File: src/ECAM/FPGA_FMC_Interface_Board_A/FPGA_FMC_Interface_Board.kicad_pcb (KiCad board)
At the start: 4 copper layers, 78.7 x 63.5 mm, 78 parts, among them IC1 ATMEGA32U4TQFP, IC2 SST25VF040B-80-4I-S2AE, IC3 NCP1117ST33T3G, IC4 LD1117S12CTR, J1 5.5x2.1mm Barrel, Q1 MOSFET-NCHANNELSMD, Q2 8MHz, U1 6SLX9TQG144, U2 ASFLMB-50.000MHZ-LC-T, X1 USB-MICROB

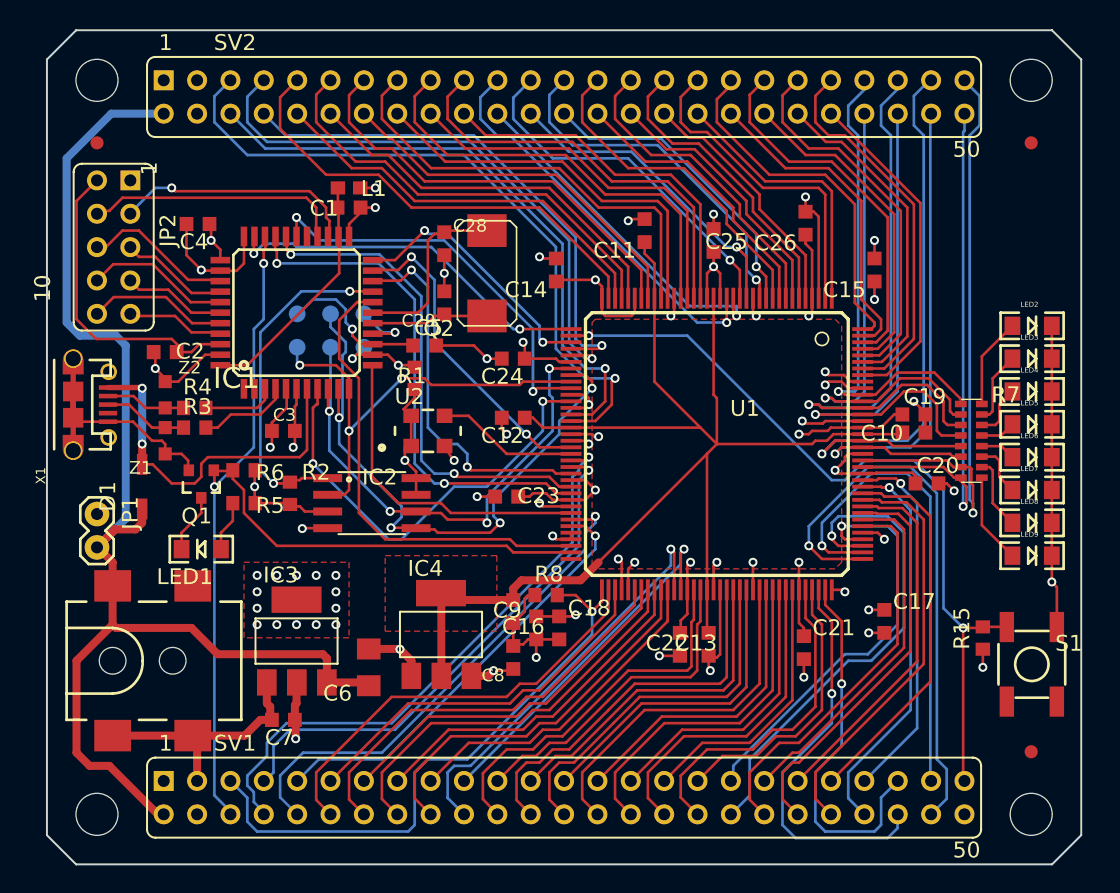
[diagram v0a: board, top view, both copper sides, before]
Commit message: added FMC connector footprint, cleaned out PCB layout
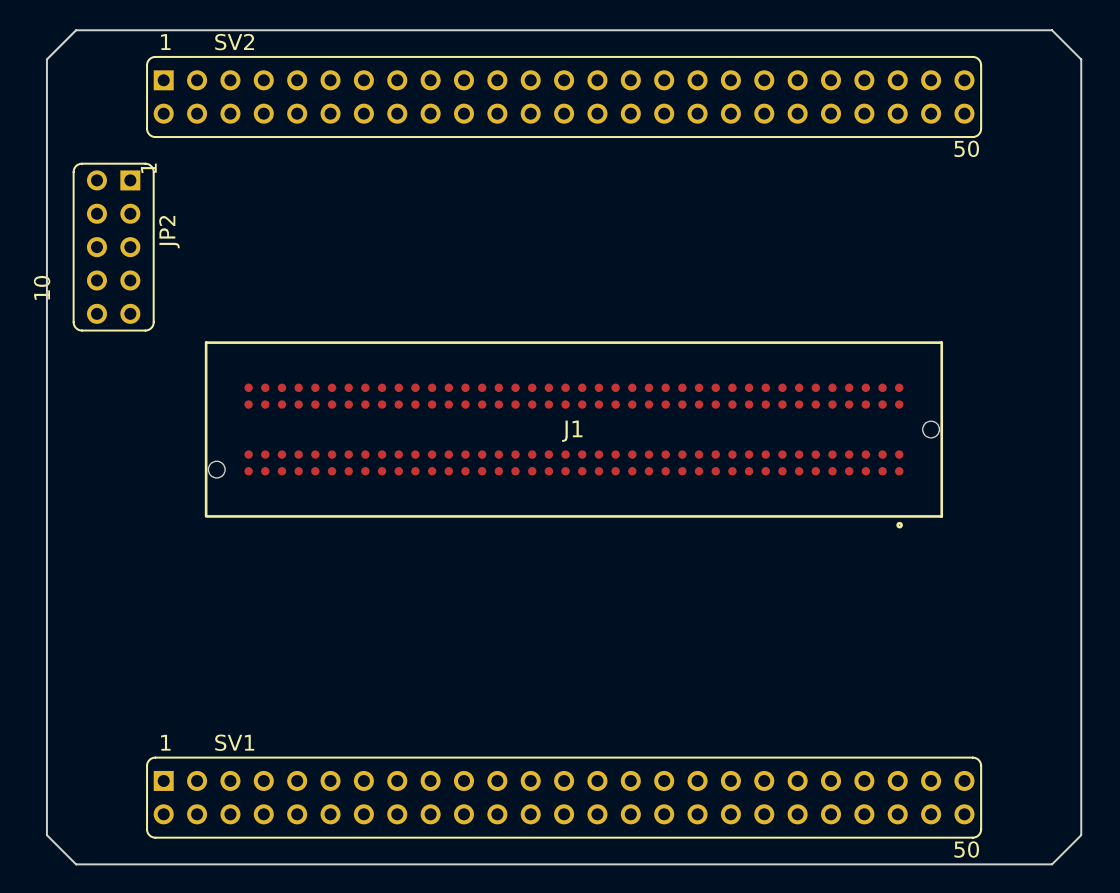
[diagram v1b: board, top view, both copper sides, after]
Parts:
- removed @HOLE0, @HOLE1, @HOLE2, @HOLE3: , 
- removed C1, C13, C18, C19, C2, C20, C21, C22, C23, C24, C25, C26, C3, C4, C5, C7, C8: 1u, v3:C0603K
- removed C10, C11, C12, C14, C15, C16, C17, C9: 10u, v3:C0603K
- removed C28, C29: 22p, v3:C0603K
- removed C6: 4u7, v3:C1206
- removed D1: MBRX120-TP, v3:SOD123
- removed IC1: ATMEGA32U4TQFP, v3:SPARKFUN-DIGITALIC_TQFP44
- removed IC2: SST25VF040B-80-4I-S2AE, v3:SO08-EIAJ
- removed IC3: NCP1117ST33T3G, v3:SOT223
- removed IC4: LD1117S12CTR, v3:SOT223
- removed JP1: M02PTH, v3:1X02
- removed JP3, JP4, JP5: FIDUCIAL1X2, v3:FIDUCIAL-1X2
- removed L1: 10uH, v3:0603
- removed LED1, LED2, LED3, LED4, LED5, LED6, LED7, LED8, LED9: LED1206, v3:LED-1206
- removed Q1: MOSFET-NCHANNELSMD, v3:SOT23-3
- removed Q2: 8MHz, v3:ABM2
- removed R1, R15, R2, R6, R8: 10K, v3:R0603
- removed R3, R4: 22, v3:R0603
- removed R5: 330, v3:R0603
- removed R7: 330, v3:CTS743C163
- removed S1: SWITCH-MOMENTARY-2SMD, v3:TACTILE_SWITCH_SMD
- removed TP1: MISO, v3:PAD.03X.05
- removed TP2: V+, v3:PAD.03X.05
- removed TP3: SCK, v3:PAD.03X.05
- removed TP4: MOSI, v3:PAD.03X.05
- removed TP5: RESET, v3:PAD.03X.05
- removed TP6: GND, v3:PAD.03X.05
- removed U1: 6SLX9TQG144, v3:TQ144
- removed U2: ASFLMB-50.000MHZ-LC-T, v3:CRYSTAL-OSC-SMD-5X3
- removed X1: USB-MICROB, v3:USB-MICROB
- removed Z1, Z2: CG0603MLC-05E, v3:CT_CN0603
- J1: value 5.5x2.1mm Barrel -> ASP-134603-01; footprint v3:POWER_JACK_SMD -> My_CONNECTORS:ASP-134604-01
- moved J1 39.3 mm to (149.2, 103.7)
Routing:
- net GND: track 178.3 -> 0.00 mm, vias 37 -> 0
- net +3V3: track 128.5 -> 0.00 mm, vias 39 -> 0
- net VCCINT: track 103.7 -> 0.00 mm
- net +5V: track 96.4 -> 0.00 mm
- net DONE: track 78.5 -> 0.00 mm, vias 2 -> 0
- net L65N_2: track 60.7 -> 0.00 mm, vias 2 -> 0
- net L31P_2: track 52.5 -> 0.00 mm, vias 1 -> 0
- net L36P_0: track 47.0 -> 0.00 mm, vias 1 -> 0
- net L31N_2: track 46.6 -> 0.00 mm, vias 1 -> 0
- net MOSI: track 46.1 -> 0.00 mm, vias 4 -> 0
- net L37P_0: track 45.8 -> 0.00 mm, vias 1 -> 0
- net L35P_0: track 45.8 -> 0.00 mm, vias 1 -> 0
- net SUSPEND: track 45.6 -> 0.00 mm, vias 1 -> 0
- net L14N_2: track 44.6 -> 0.00 mm, vias 1 -> 0
- net TCK: track 43.7 -> 0.00 mm, vias 1 -> 0
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- removed copper zone on F.Cu, net +3V3
- removed copper zone on Power, net +3V3
- removed copper zone on F.Cu, net VCCINT
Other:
- board text removed: "+"
- board text removed: "-"
- board text removed: "4.8V-12V"
- board text removed: "Reset"

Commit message: small board update
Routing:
- net +3V3: track 0.00 -> 58.2 mm
- net +5V: track 0.00 -> 55.5 mm
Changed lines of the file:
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@@
     (thickness 1.6)
     (drawings 125)
-    (tracks 0)
+    (tracks 16)
     (zones 0)
     (modules 4)
@@
     (mod_text_size 1 1)
     (mod_text_width 0.15)
-    (pad_size 1.524 1.524)
-    (pad_drill 0.762)
+    (pad_size 0.64 0.64)
+    (pad_drill 0)
     (pad_to_mask_clearance 0.051)
     (solder_mask_min_width 0.25)
@@
   (gr_line (start 187.8711 75.4761) (end 185.6486 73.2536) (layer Edge.Cuts) (width 0.15))
   (gr_line (start 187.8711 134.5311) (end 185.6486 136.7536) (layer Edge.Cuts) (width 0.15))
+  (segment (start 120.5611 80.68123) (end 118.6 82.64233) (width 0.25) (layer Top) (net 1))
+  (segment (start 120.5611 79.6036) (end 120.5611 80.68123) (width 0.25) (layer Top) (net 1))
+  (segment (start 118.6 96.93641) (end 116.20001 99.3364) (width 0.25) (layer Top) (net 1))
+  (segment (start 118.6 82.64233) (end 118.6 96.93641) (width 0.25) (layer Top) (net 1))
+  (segment (start 116.20001 99.3364) (end 116.4 99.53639) (width 0.25) (layer Top) (net 1))
+  (segment (start 119.799101 132.181601) (end 120.5611 132.9436) (width 0.25) (layer Top) (net 1))
+  (segment (start 119.108101 131.490601) (end 119.799101 132.181601) (width 0.25) (layer Top) (net 1))
+  (segment (start 116.999099 131.490601) (end 119.108101 131.490601) (width 0.25) (layer Top) (net 1))
+  (segment (start 116.4 130.891502) (end 116.999099 131.490601) (width 0.25) (layer Top) (net 1))
+  (segment (start 116.4 99.53639) (end 116.4 130.891502) (width 0.25) (layer Top) (net 1))
+  (segment (start 117.259101 132.181601) (end 116.731601 132.181601) (width 0.25) (layer Top) (net 4))
+  (segment (start 118.0211 132.9436) (end 117.259101 132.181601) (width 0.25) (layer Top) (net 4))
+  (segment (start 116.731601 132.181601) (end 115.75 131.2) (width 0.25) (layer Top) (net 4))
+  (segment (start 115.75 131.2) (end 115.75 99.15) (width 0.25) (layer Top) (net 4))
+  (segment (start 118.0211 96.8789) (end 118.0211 79.6036) (width 0.25) (layer Top) (net 4))
+  (segment (start 115.75 99.15) (end 118.0211 96.8789) (width 0.25) (layer Top) (net 4))
   (zone (net 2) (net_name GND) (layer Ground) (hatch edge 0.508)
     (priority 6)
     (connect_pads (clearance 0.4064))
     (min_thickness 0.4064)
-    (fill (arc_segments 32) (thermal_gap 0.4564) (thermal_bridge_width 0.4564))
+    (fill yes (arc_segments 32) (thermal_gap 0.4564) (thermal_bridge_width 0.4564))
     (polygon
       (pts
